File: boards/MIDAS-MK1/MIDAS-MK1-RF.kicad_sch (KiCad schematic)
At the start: 15 parts, among them IC401 TESEO-LIV3F, J401 Conn_Coaxial, J402 Conn_Coaxial, U401 RFM96W-433S2, U402 BGA725L6E6327FTSA1

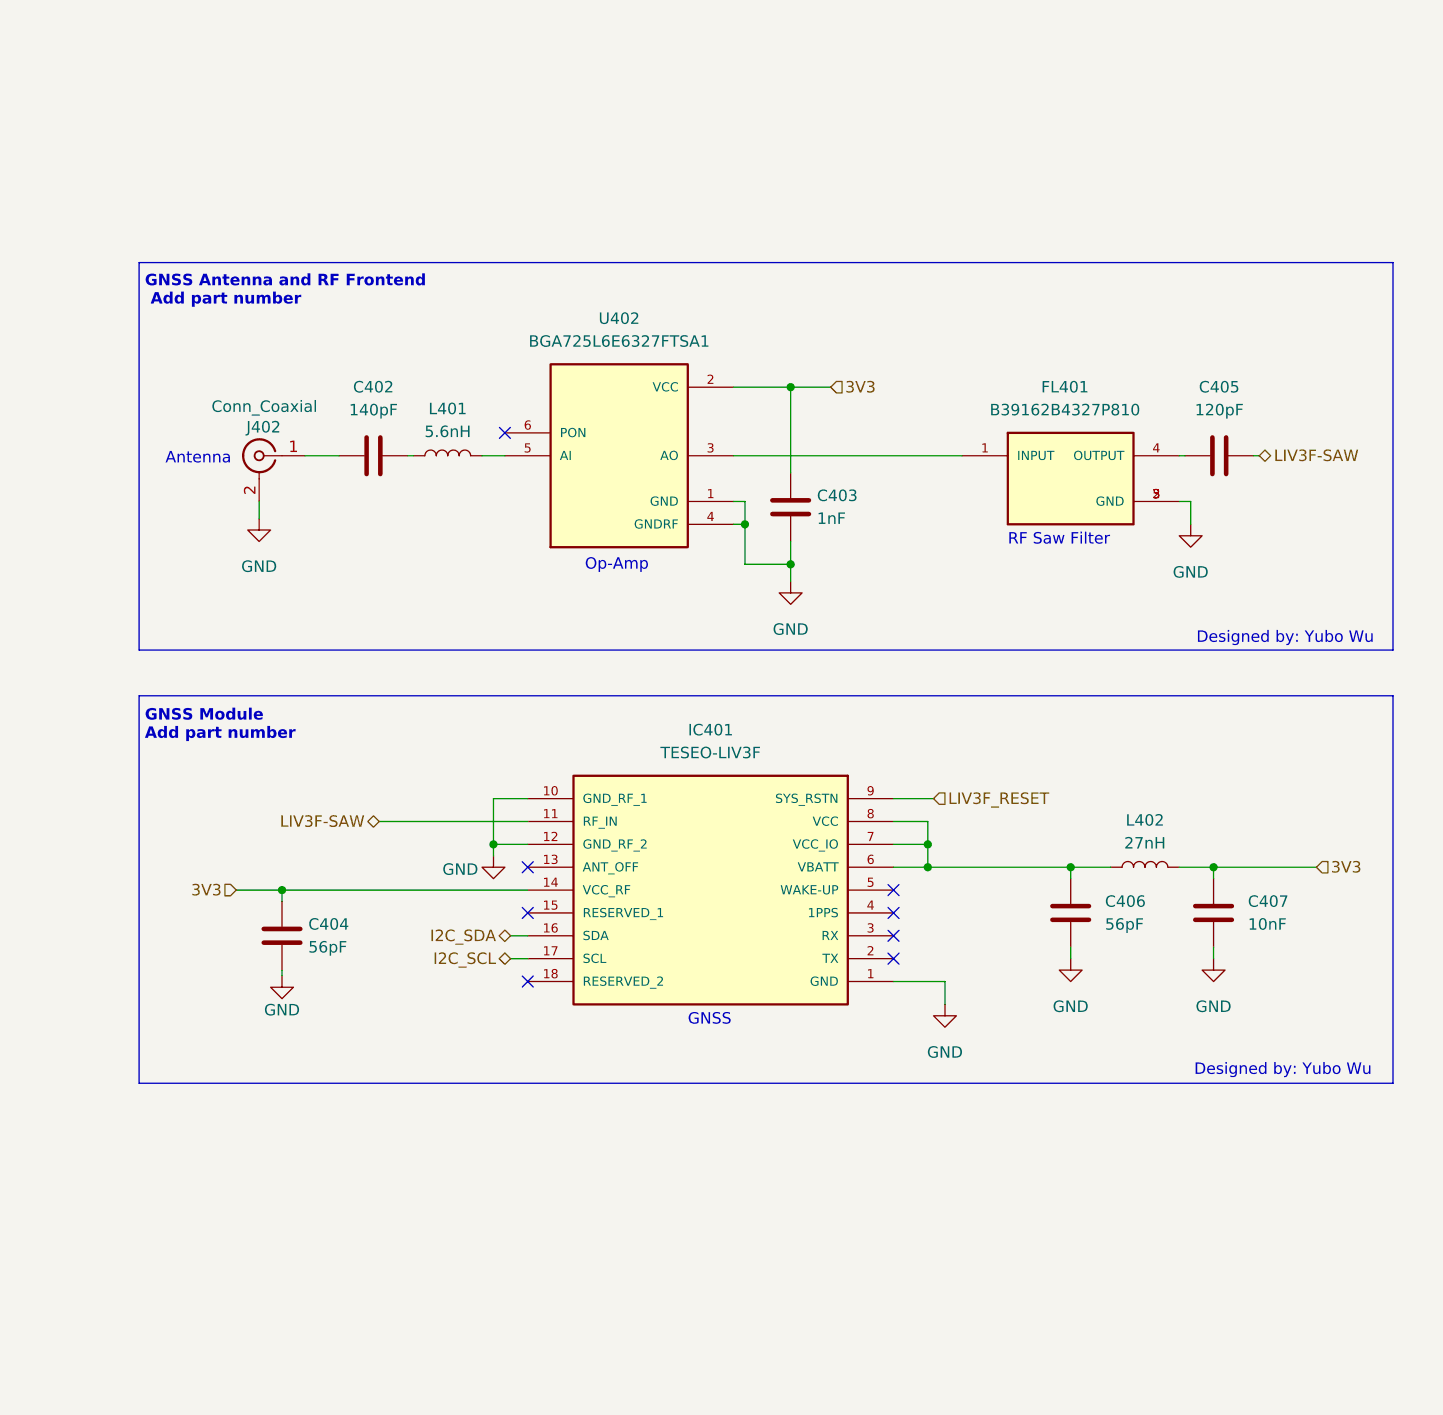
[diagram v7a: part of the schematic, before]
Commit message: Added new symbols with correct fps, need to connect
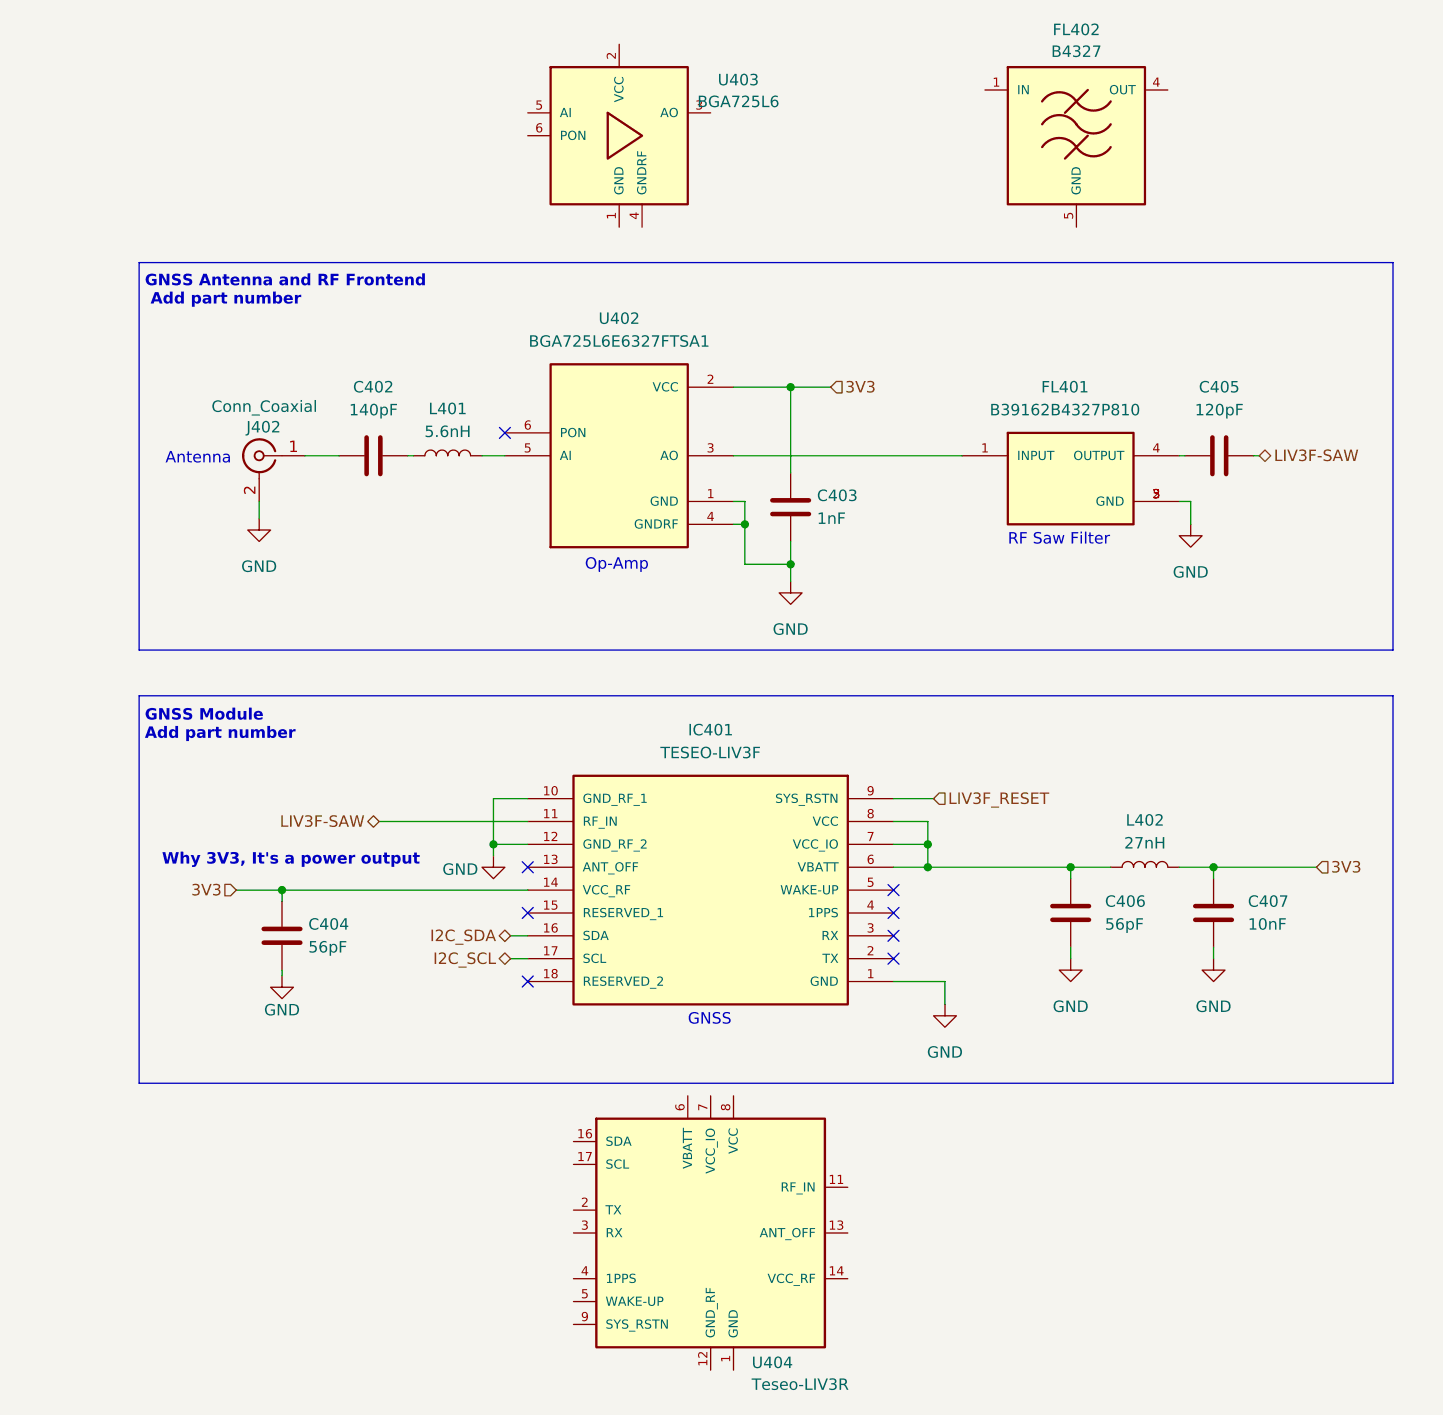
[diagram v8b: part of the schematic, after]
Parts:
- added FL402: B4327, RF_Filter_Qualcomm:SMD-5, symbol RF_Filter_Qualcomm:B4327
- added U403: BGA725L6, RF_Amplifier_Infineon:TSNP-6-2, symbol RF_Amplifier_Infineon:BGA725L6
- added U404: Teseo-LIV3R, RF_GPS_ST:Teseo-LIV3R, symbol RF_GPS_ST:Teseo-LIV3R
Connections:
- net GND: now also FL402.2 (GND), FL402.3 (GND), FL402.5 (GND)
- new net: U404.15 (RESERVED), U404.18 (RESERVED)
- new net GND_RF: U404.10 (GND_RF), U404.12 (GND_RF)
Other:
- note added: "Why 3V3, It's a power output"
- note removed: "Designed by: Yubo Wu"
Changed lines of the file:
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@@
     (rev "A")
     (company "Illinois Space Society")
+    (comment 4 "Contributors: Yubo Wu")
   )
